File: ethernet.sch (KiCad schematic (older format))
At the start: 52 parts, among them J2 L834-1G1T-S7, U6 KSZ9031RNXCA, Y1 ABM8G-25.000MHZ-18-D2Y-T

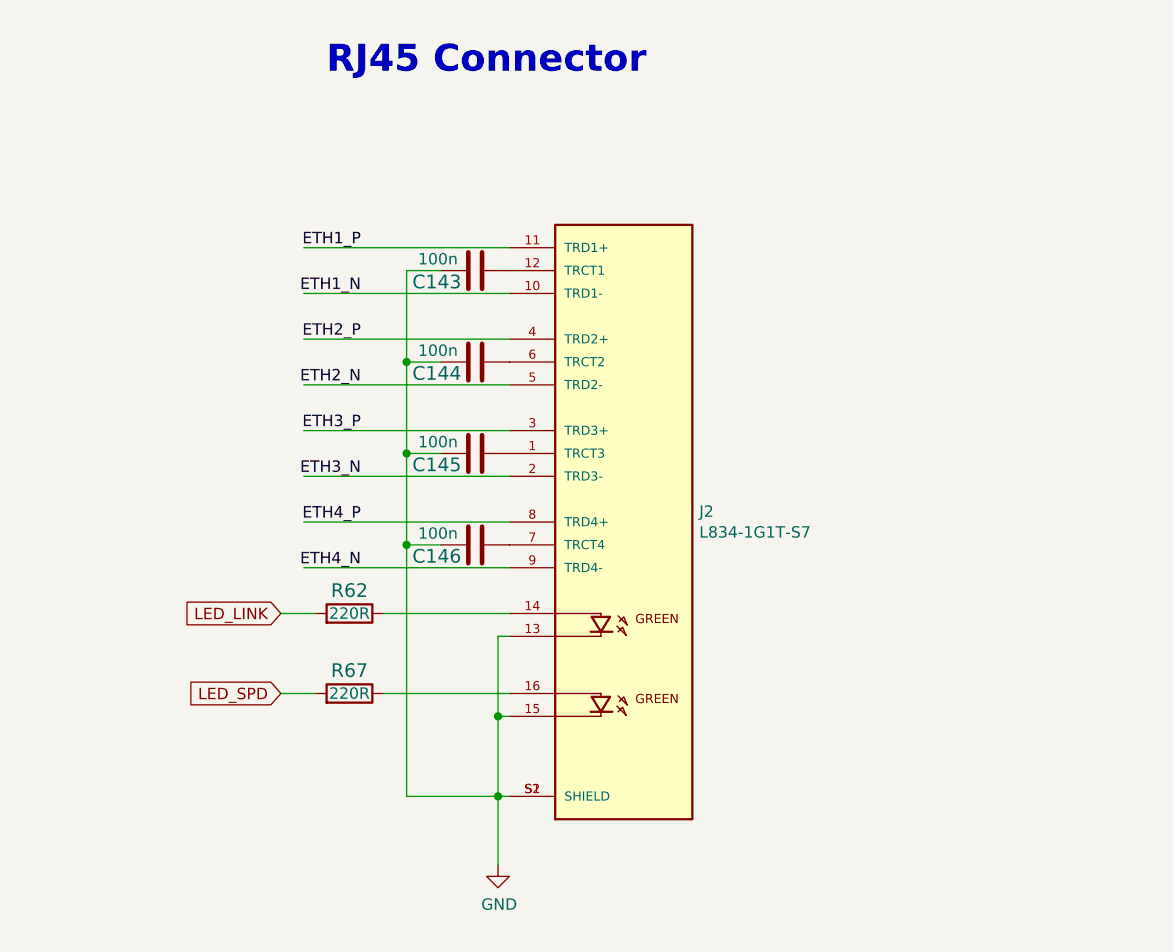
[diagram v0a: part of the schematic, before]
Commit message: Update ETH connector
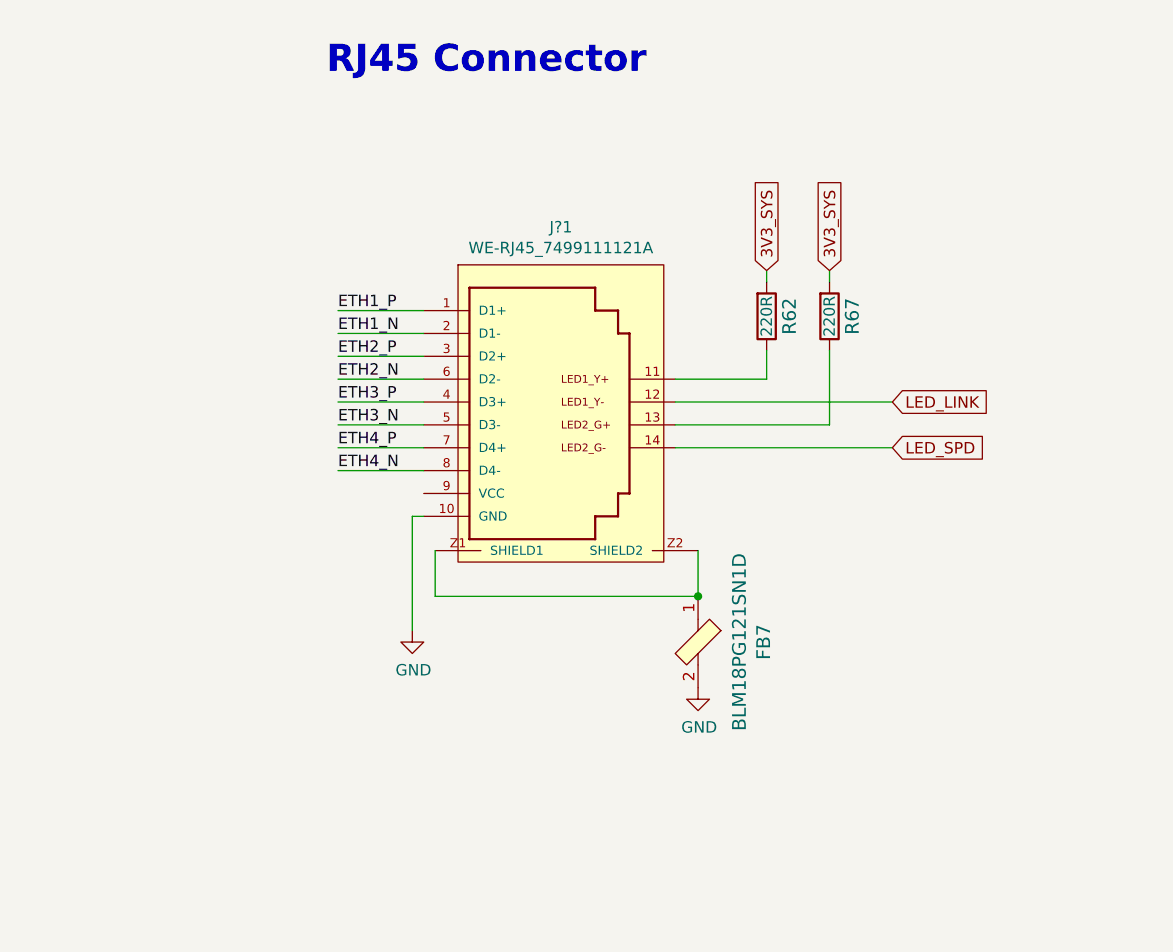
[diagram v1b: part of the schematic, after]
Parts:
- removed C143, C144, C145, C146: C_100n_0402, artix-dc-scm-footprints:0402-cap, symbol lpddr4-test-board:C_100n_0402_16V
- removed J2: L834-1G1T-S7, artix-dc-scm-footprints:BEL_L834-1G1T-S7, symbol antmicroModularConnectorsJacksWithMagnetics:L834-1G1T-S7
- added FB7: BLM18PG121SN1D, artix-dc-scm-footprints:0603-res, symbol antmicroFerriteBeadsandChips:BLM18PG121SN1D
- added J?1: WE-RJ45_7499111121A, antmicro-footprints:7499111121A, symbol antmicroModularConnectorsJacksWithMagnetics:WE-RJ45_7499111121A
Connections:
- wire segments 244 -> 238

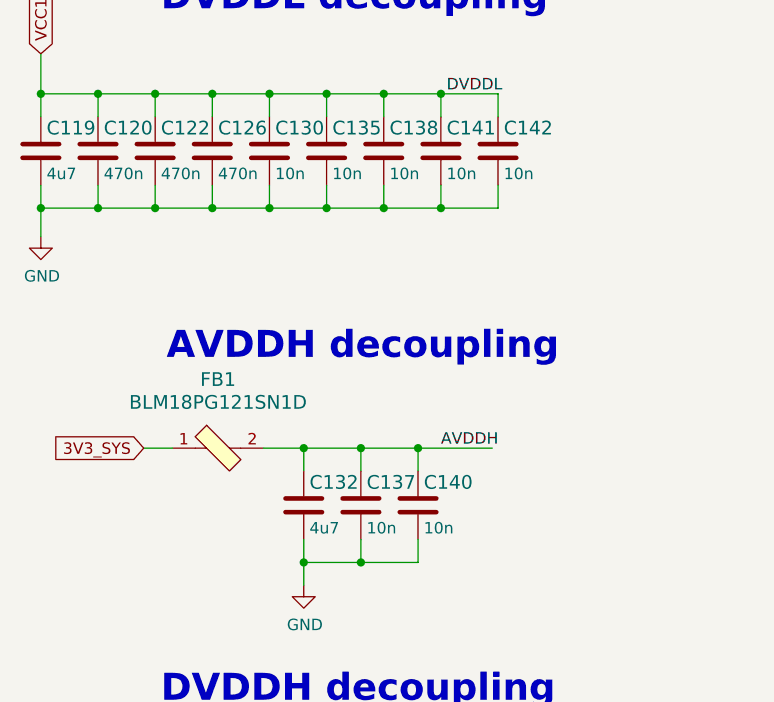
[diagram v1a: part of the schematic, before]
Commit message: Update footprint links
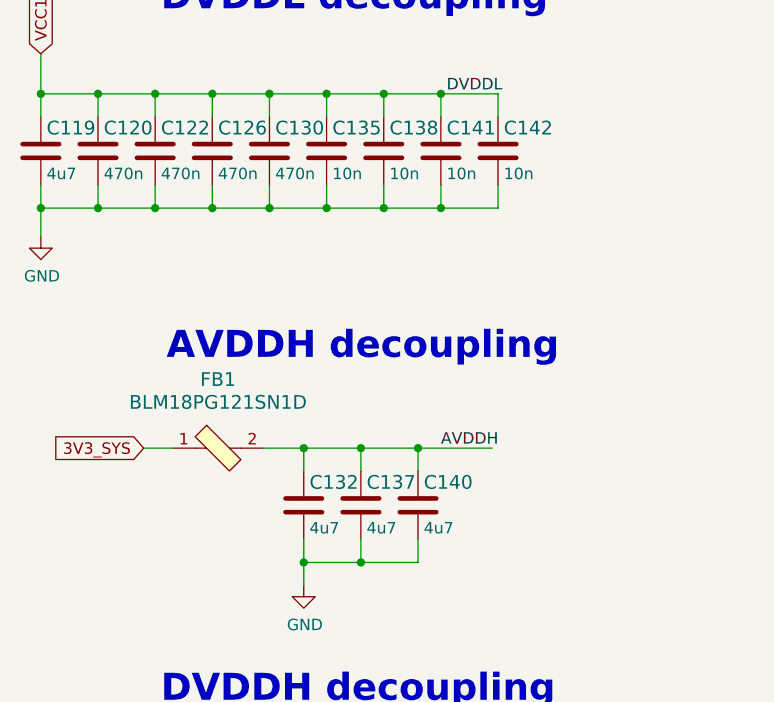
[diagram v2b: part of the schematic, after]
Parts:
- C119, C120, C121, C123, C124, C125, C127, C129, C131, C132, C133, C134, C136, C139: footprint artix-dc-scm-footprints:0402-cap -> lpddr4-test-board-footprints:0402-cap
- C122, C126, C135, C138, C141, C142, C147, C148: footprint artix-dc-scm-footprints:0402-cap -> antmicro-footprints:0402-cap
- C128: footprint artix-dc-scm-footprints:0402-cap -> lpddr4-test-board-footprints:0402-cap; MPN 0402X104K6R3CT -> MC0402B104K160CT; Manufacturer Walsin -> MULTICOMP
- C130: footprint artix-dc-scm-footprints:0402-cap -> antmicro-footprints:0402-cap; MPN 04025G103ZAT2A -> C1005X5R1E474M050BB; Manufacturer AVX -> TDK; Val 10n -> 470n
- C137: footprint artix-dc-scm-footprints:0402-cap -> lpddr4-test-board-footprints:0402-cap; MPN 04025G103ZAT2A -> GRM155R61A475MEAAD; Manufacturer AVX -> MURATA; Val 10n -> 4u7
- C140: footprint artix-dc-scm-footprints:0402-cap -> antmicro-footprints:0402-cap; MPN 04025G103ZAT2A -> GRM155R61A475MEAAD; Manufacturer AVX -> MURATA; Val 10n -> 4u7
- FB1, FB2, FB3, FB7: footprint artix-dc-scm-footprints:0603-res -> antmicro-footprints:0603-res
- R62, R67: footprint artix-dc-scm-footprints:0402-res -> lpddr4-test-board-footprints:0402-res
- R68: footprint artix-dc-scm-footprints:0402-res -> antmicro-footprints:0402-res
- R69: footprint artix-dc-scm-footprints:0402-res -> antmicro-footprints:0402-res; Manufacturer Multicomp -> MULTICOMP
- U6: footprint artix-dc-scm-footprints:QFN-48-Microchip-QFN77-48LD-PL-2 -> antmicro-footprints:QFN-48-Microchip-QFN77-48LD-PL-2
- Y1: footprint artix-dc-scm-footprints:KX-7 -> lpddr4-test-board-footprints:KX-7

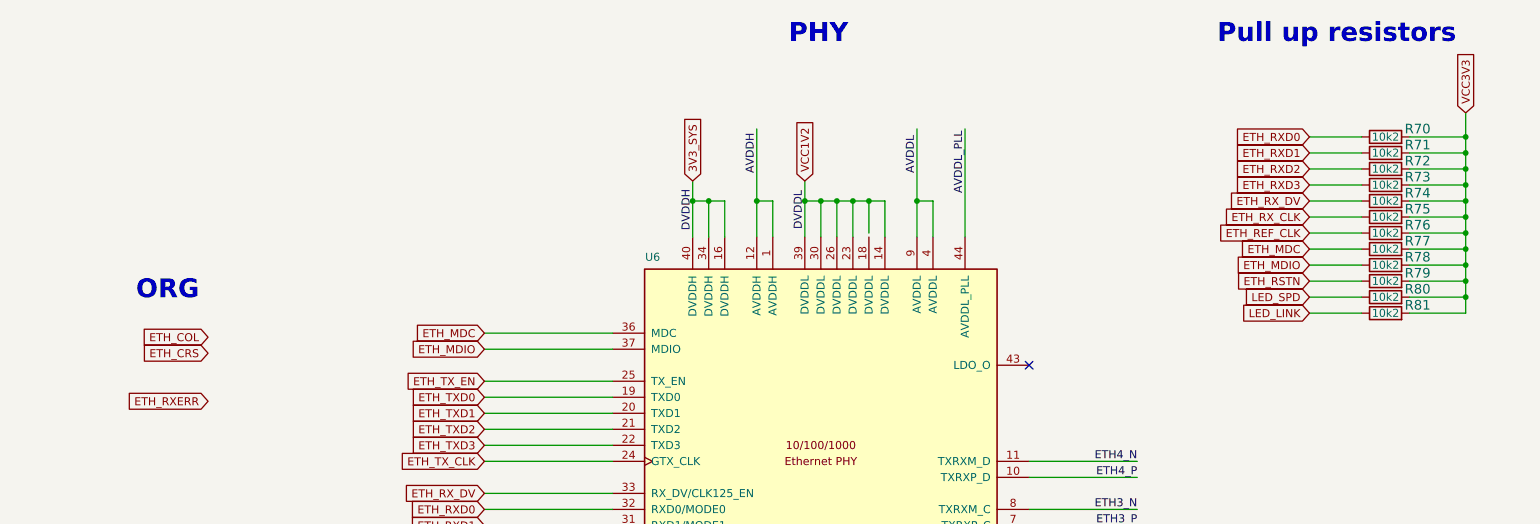
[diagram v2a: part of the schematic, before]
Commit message: Update PCB layout DRC clean
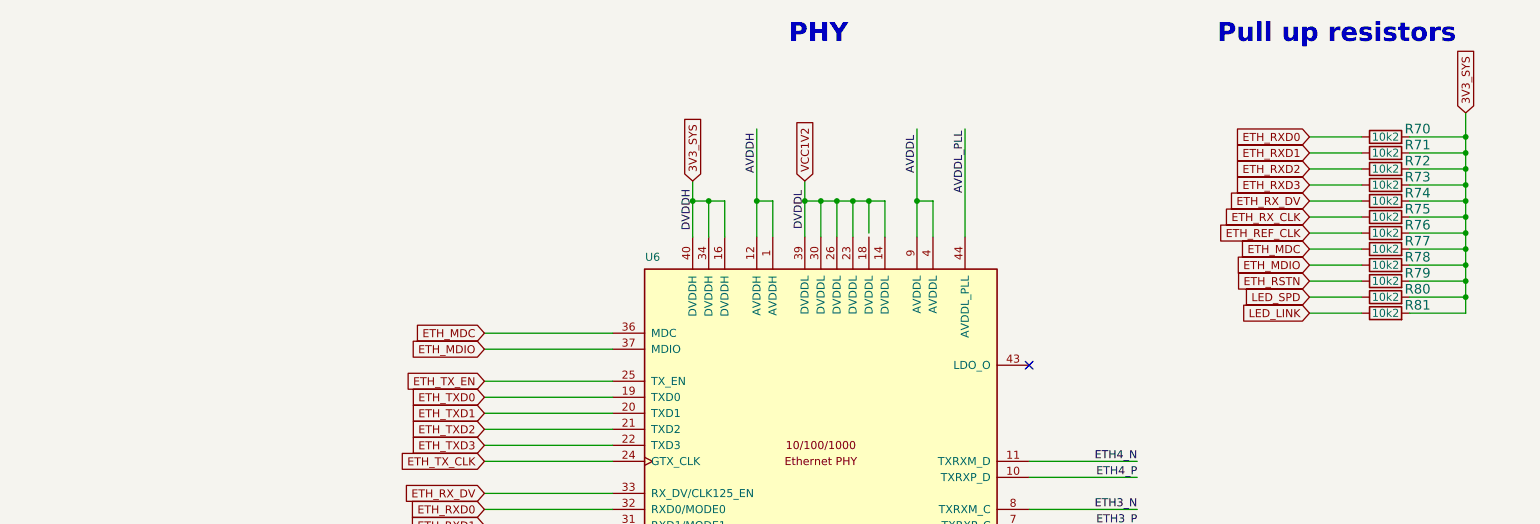
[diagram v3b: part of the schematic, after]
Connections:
- net VCC3V3 is gone; now on net 3V3_SYS: R70.2, R71.2, R72.2, R73.2, R74.2, R75.2, R76.2, R77.2, R78.2, R79.2, R80.2, R81.2
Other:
- note removed: "ORG"
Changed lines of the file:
@@
 	1    0    0    -1
 $EndComp
-Text GLabel 14900 1575 1    50   Input ~ 0
-VCC3V3
 Text Notes 13350 1150 0    118  ~ 24
 Pull up resistors
@@
 Text GLabel 8775 3950 0    50   Input ~ 0
 ETH_RX_DV
-Text GLabel 7050 3375 0    50   Input ~ 0
-ETH_RXERR
-Text GLabel 7050 2975 0    50   Input ~ 0
-ETH_COL
-Text GLabel 7050 3075 0    50   Input ~ 0
-ETH_CRS
 Text GLabel 8775 2950 0    50   Input ~ 0
 ETH_MDC
 Text GLabel 8775 3050 0    50   Input ~ 0
 ETH_MDIO
-Text Notes 6600 2750 0    118  ~ 24
-ORG
 Text GLabel 10075 2000 1    50   Input ~ 0
 3V3_SYS
@@
 Wire Wire Line
 	9250 8425 8875 8425
+Text GLabel 14900 1575 1    50   Input ~ 0
+3V3_SYS
 $EndSCHEMATC
